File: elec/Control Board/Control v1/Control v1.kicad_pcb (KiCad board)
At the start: 2 copper layers, 126.3 x 160 mm, 194 parts, among them J1 DB9_Female_MountingHoles, J103 Screw_Terminal_01x02, J106 Conn_01x04, J107 Conn_01x07, J11 Screw_Terminal_01x02, J111 Conn_01x08, J13 DB25_Female_MountingHoles, J14 Conn_01x04, J15 Conn_01x05, J16 Conn_01x04, J17 Conn_01x07, J18 Conn_01x04_Pin, J19 RJ12_6P6C_HORZ, J2 Conn_01x08, J20 0.100_2Pin, J201 0.100_2Pin, J202 Conn_01x04, J21 0.100_2Pin, J22 Conn_01x04, J23 0.100_2Pin, J24 0.100_2Pin, J25 Conn_01x04, J3 Conn_01x08, J302 0.100_2Pin, J4 Conn_01x08, J5 Conn_01x08, J6 Conn_01x08, J7 Conn_02x18_Odd_Even, J8 Conn_01x10_MountingPin, J9 Conn_02x12_Odd_Even, Q1 BSS138, Q10 BSS138, Q2 NCE01P30K, Q3 BSS138, Q301 BSS138, Q302 BSS138, Q303 BSS138, Q304 BSS138, Q4 BSS138, Q5 BSS138, Q6 BSS138, Q7 BSS138, Q8 BSS138, Q9 BSS138

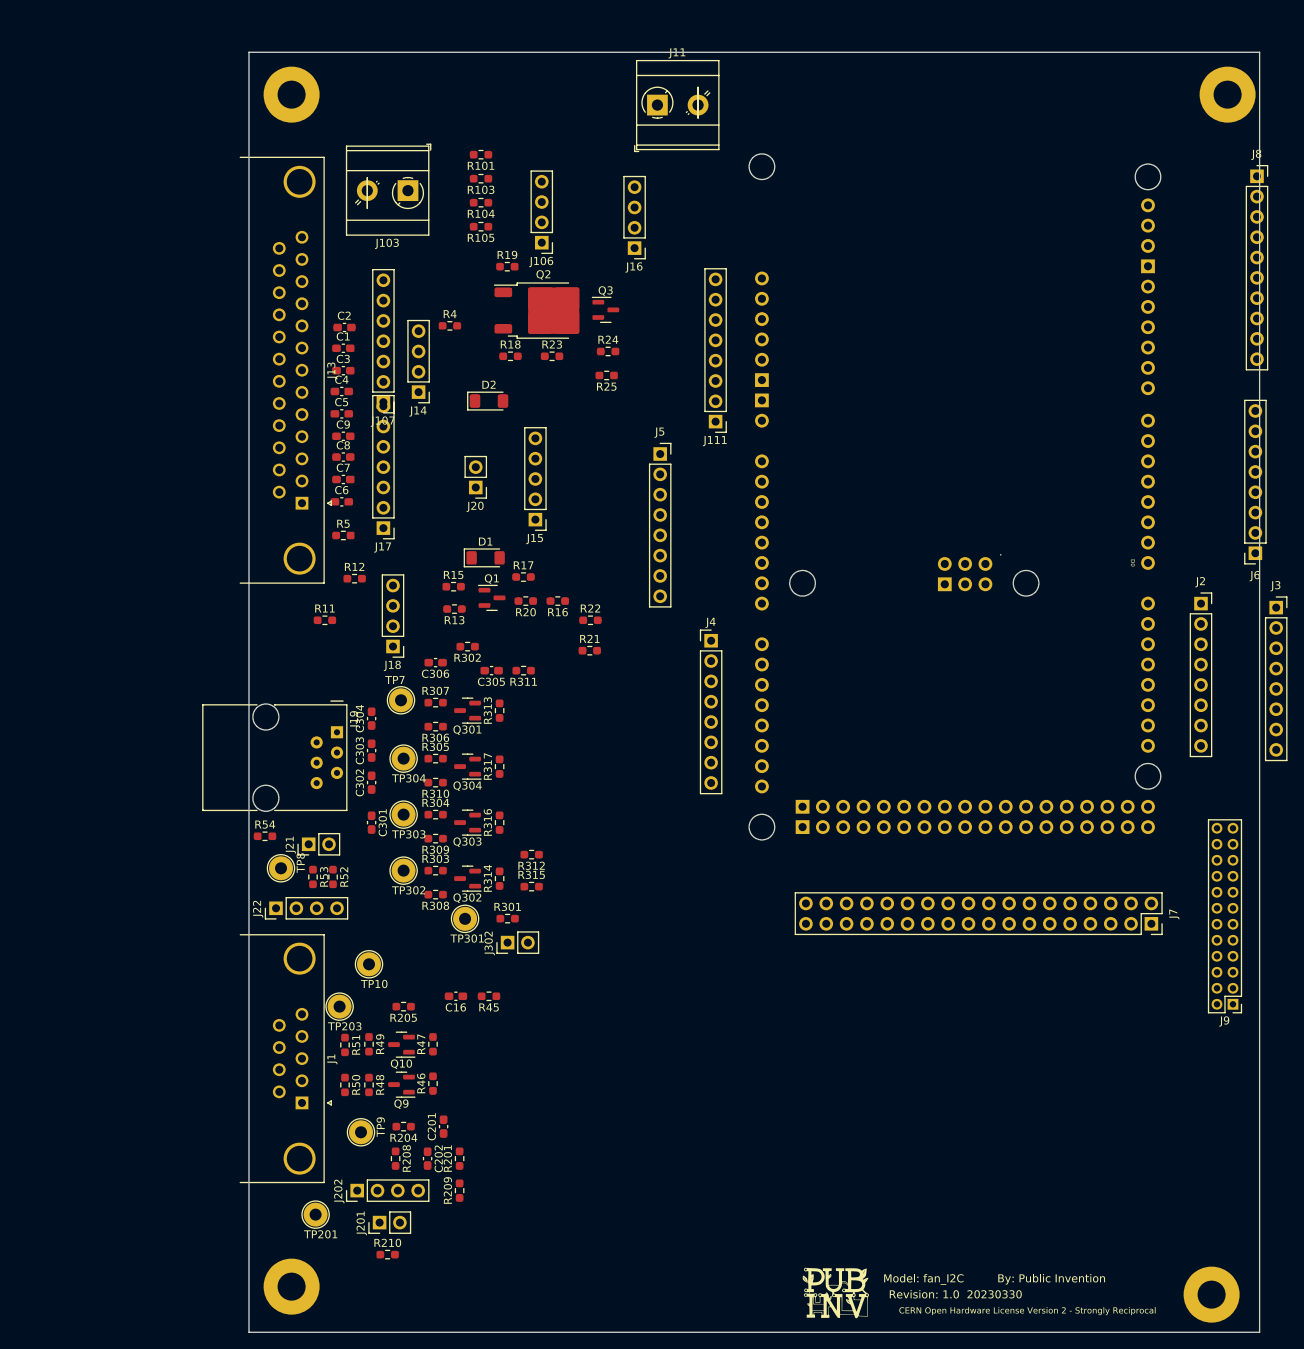
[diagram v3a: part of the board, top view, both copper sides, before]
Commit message: Update schematic for MCP9600 I2C thermocouple.
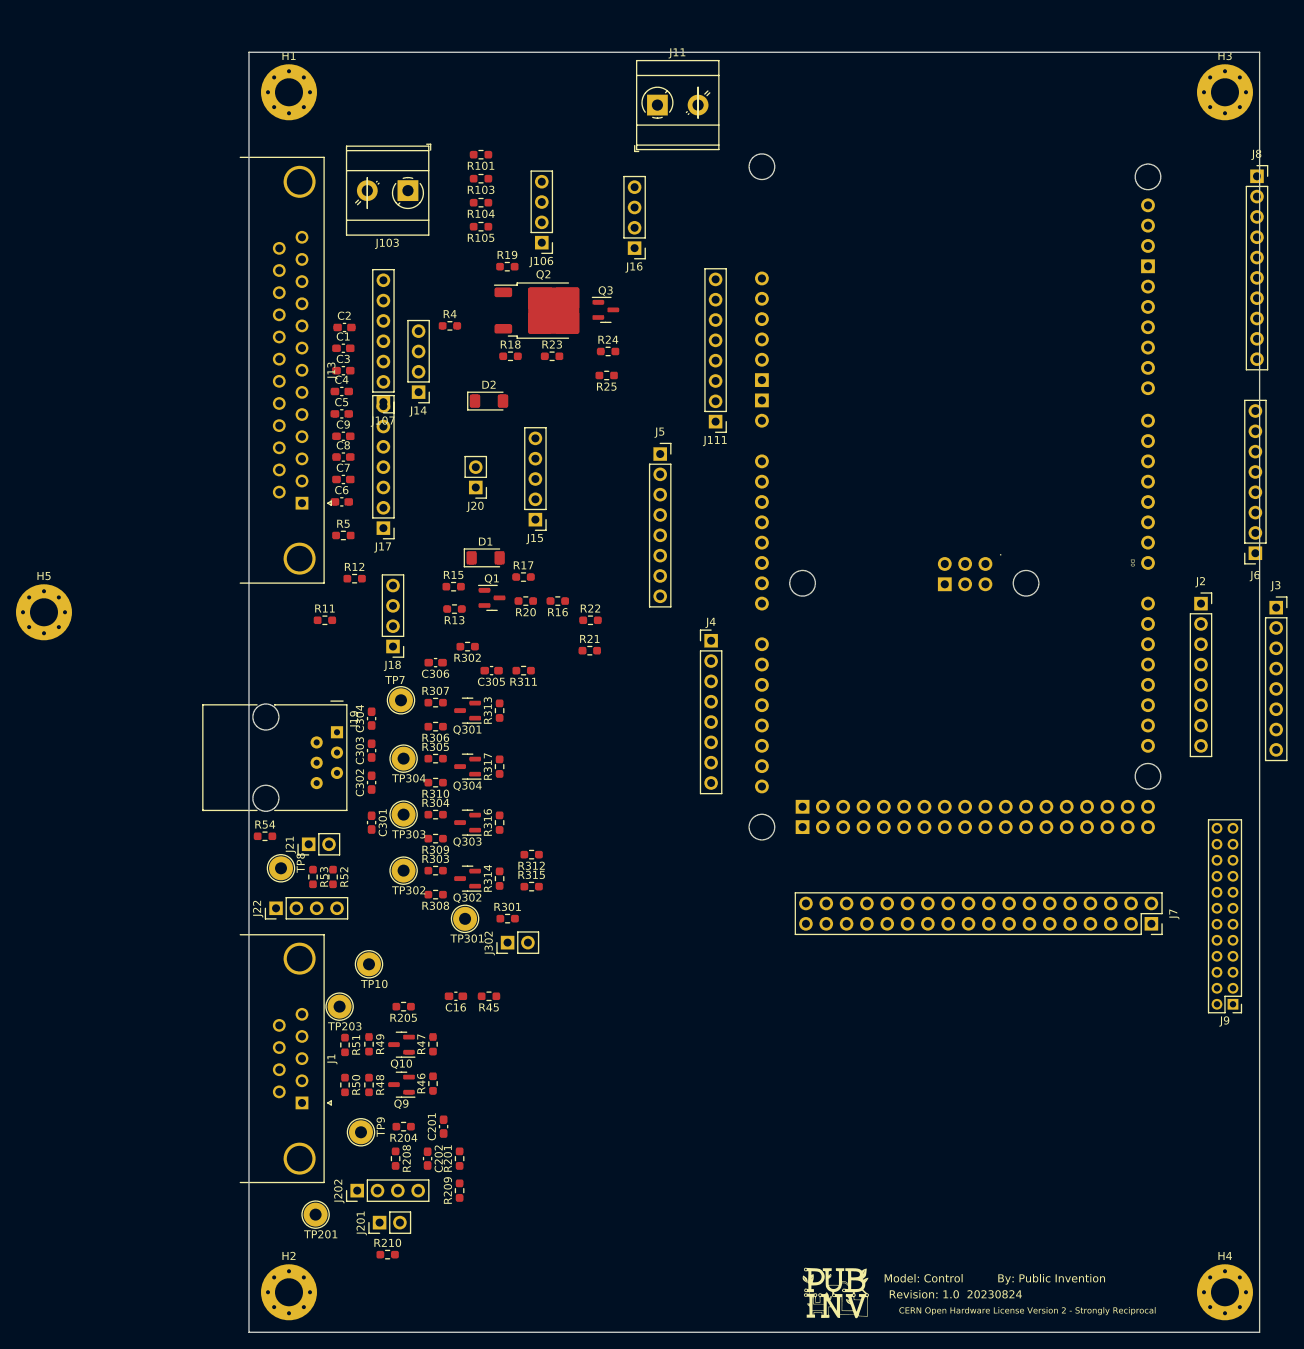
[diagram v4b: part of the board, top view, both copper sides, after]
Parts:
- removed ? (x4): , 
- added H1: MountingHole_Pad_3.5mm, PubInv_KiCad_PCB:MountingHole_3.5mm_Pad_Via, F.Cu at (55.0, 55.0)
- added H2: MountingHole_Pad_3.5mm, PubInv_KiCad_PCB:MountingHole_3.5mm_Pad_Via, F.Cu at (55.0, 205.0)
- added H3: MountingHole_Pad_3.5mm, PubInv_KiCad_PCB:MountingHole_3.5mm_Pad_Via, F.Cu at (172.0, 55.0)
- added H4: MountingHole_Pad_3.5mm, PubInv_KiCad_PCB:MountingHole_3.5mm_Pad_Via, F.Cu at (172.0, 205.0)
- added H5: MountingHole_Pad_3.5mm, PubInv_KiCad_PCB:MountingHole_3.5mm_Pad_Via, F.Cu at (24.4, 120.0)
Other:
- board text added: "Model: Control"
- board text added: "Revision: 1.0 20230824"
- board text removed: "Model: fan_I2C"
- board text removed: "Revision: 1.0 20230330"

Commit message: More update schematic for MCP9600 I2C thermocouple.
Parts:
- added JP14: SolderJumper_3_Bridged12, Jumper:SolderJumper-3_P1.3mm_Bridged12_RoundedPad1.0x1.5mm, F.Cu at (320.3, 113.3)
- added JP15: MAX31850K, PubInv_KiCad_PCB:Adafruit_MAX31850K_Module, F.Cu at (297.4, 148.9)
- added JP16: MAX31855, PubInv_KiCad_PCB:Adafruit_MAX31855_Module, F.Cu at (264.2, 75.2)
- added JP17: MAX31855, PubInv_KiCad_PCB:Adafruit_MAX31855_Module, F.Cu at (286.6, 75.2)
- added JP18: MAX31855, PubInv_KiCad_PCB:Adafruit_MAX31855_Module, F.Cu at (309.0, 75.2)
- added JP19: MCP9600, PubInv_KiCad_PCB:Adafruit_MCP9600_Module, F.Cu at (261.8, 105.8)
- added JP20: MCP9600_, PubInv_KiCad_PCB:Adafruit_MCP9600_Module, F.Cu at (261.8, 128.3)
- added JP21: MCP9600, PubInv_KiCad_PCB:Adafruit_MCP9600_Module, F.Cu at (261.8, 150.8)
- added R10: 1K, Resistor_SMD:R_0603_1608Metric_Pad0.98x0.95mm_HandSolder, F.Cu at (319.6, 116.6)
- added R12: 1K, Resistor_SMD:R_0603_1608Metric_Pad0.98x0.95mm_HandSolder, F.Cu at (319.6, 119.1)
- added R13: 1K, Resistor_SMD:R_0603_1608Metric_Pad0.98x0.95mm_HandSolder, F.Cu at (319.6, 121.6)
- added R14: 1K, Resistor_SMD:R_0603_1608Metric_Pad0.98x0.95mm_HandSolder, F.Cu at (319.6, 124.1)
- added R15: 1K, Resistor_SMD:R_0603_1608Metric_Pad0.98x0.95mm_HandSolder, F.Cu at (319.6, 126.6)
- added R16: 1K, Resistor_SMD:R_0603_1608Metric_Pad0.98x0.95mm_HandSolder, F.Cu at (319.6, 129.2)
- added R17: 1K, Resistor_SMD:R_0603_1608Metric_Pad0.98x0.95mm_HandSolder, F.Cu at (319.6, 131.7)
- added R18: 1K, Resistor_SMD:R_0603_1608Metric_Pad0.98x0.95mm_HandSolder, F.Cu at (319.6, 134.2)
- added R19: 1R0, Resistor_SMD:R_0603_1608Metric_Pad0.98x0.95mm_HandSolder, F.Cu at (269.1, 78.9)
- added R20: 1R0, Resistor_SMD:R_0603_1608Metric_Pad0.98x0.95mm_HandSolder, F.Cu at (290.2, 91.0)
- added TP3: +VccMAX31850_2, TestPoint:TestPoint_Loop_D2.54mm_Drill1.5mm_Beaded, F.Cu at (320.0, 137.9)
- added TP4: +VccMAX31850_3, TestPoint:TestPoint_Loop_D2.54mm_Drill1.5mm_Beaded, F.Cu at (320.0, 143.0)
- added TP5: +VccMAX3185, TestPoint:TestPoint_Loop_D2.54mm_Drill1.5mm_Beaded, F.Cu at (264.4, 80.1)
- added TP6: +VccMCP9600, TestPoint:TestPoint_Loop_D2.54mm_Drill1.5mm_Beaded, F.Cu at (290.6, 87.2)
- JP10, JP9: value MAX31855 -> MAX31850K; footprint PubInv_KiCad_PCB:Adafruit_MAX31855_Module -> PubInv_KiCad_PCB:Adafruit_MAX31850K_Module
- JP11, JP12, JP13: value MAX31865 -> SolderJumper_3_Bridged12; footprint PubInv_KiCad_PCB:Adafruit_MAX31865_Module -> Jumper:SolderJumper-3_P1.3mm_Bridged12_RoundedPad1.0x1.5mm
- JP5, JP6, JP7: value MAX31850K -> SolderJumper_3_Bridged12; footprint PubInv_KiCad_PCB:Adafruit_MAX31850K_Module -> Jumper:SolderJumper-3_P1.3mm_Bridged12_RoundedPad1.0x1.5mm
- JP8: value MAX31855 -> SolderJumper_3_Bridged12; footprint PubInv_KiCad_PCB:Adafruit_MAX31855_Module -> Jumper:SolderJumper-3_P1.3mm_Bridged12_RoundedPad1.0x1.5mm
- moved JP7 91.1 mm to (320.3, 94.1)
- moved JP5 88.6 mm to (320.3, 86.4)
- moved JP6 88.0 mm to (320.3, 90.3)
- moved JP11 59.5 mm to (320.3, 101.8)
- moved JP8 58.3 mm to (320.3, 97.9)
- moved JP12 35.4 mm to (320.3, 105.6)
- moved JP13 22.6 mm to (320.3, 109.5)
- moved JP10 18.0 mm to (297.4, 126.7)
- moved JP9 13.8 mm to (297.4, 104.5)
- moved TP2 13.8 mm to (266.0, 49.0)
- renumbered R10 to R11, R11 to R21, R12 to R22, R13 to R23, R15 to R25, R16 to R26, R17 to R27, R18 to R28, R19 to R29, R20 to R30, R21 to R31, R22 to R32, R23 to R33, R24 to R34, R25 to R35, R26 to R36, R27 to R37, R28 to R38, R29 to R39, R30 to R40, R31 to R41, R32 to R42, R33 to R43, R34 to R44, R35 to R45, R36 to R46, R37 to R47, R38 to R48, R39 to R49, R40 to R50, R41 to R51, R42 to R52, R43 to R53, R44 to R54, R45 to R55, R46 to R56, R47 to R57, R48 to R58, R49 to R59, R7 to R6, R50 to R60, R51 to R61, R52 to R62, R53 to R63, R54 to R64, R6 to R7, TP6 to TP10, TP7 to TP11, TP8 to TP12, TP9 to TP13, TP10 to TP14, TP3 to TP7, TP4 to TP8, TP5 to TP9
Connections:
- JP1 pad 1: GND -> /Thermocouple Amplifier with 1-Wire Breakout Board - MAX31850K/+VccMAX31850
- JP1 pad 3: /Thermocouple Amplifier with 1-Wire Breakout Board - MAX31850K/+VccMAX31850 -> GND
- JP10 pad 1: unconnected-(JP10-Pad1) -> ONE_WIRE_TC
- JP10 pad 2: unconnected-(JP10-Pad2) -> Net-(JP10-Pad2)
- JP10 pad 3: unconnected-(JP10-Pad3) -> Net-(JP10-Pad3)
- JP10 pad 4: unconnected-(JP10-Pad4) -> Net-(JP10-Pad4)
- JP10 pad 5: unconnected-(JP10-Pad5) -> Net-(JP10-Pad5)
- JP10 pad 6: unconnected-(JP10-Pad6) -> Net-(JP10-Pad6)
- JP10 pad 8: (no net) -> GND
- JP11 pad 1: +5V -> GND
- JP11 pad 2: /Thermocouple Amplifier SPI breakout board - MAX31865/+3.3V_MAX31856 -> Net-(JP11-C)
- JP11 pad 3: GND -> /Thermocouple Amplifier with 1-Wire Breakout Board - MAX31850K/+VccMAX31850
- JP12 pad 1: unconnected-(JP12-Pad1) -> GND
- JP12 pad 2: unconnected-(JP12-Pad2) -> Net-(JP12-C)
- JP12 pad 3: unconnected-(JP12-Pad3) -> /Thermocouple Amplifier with 1-Wire Breakout Board - MAX31850K/+VccMAX31850
- JP13 pad 1: unconnected-(JP13-Pad1) -> /Thermocouple Amplifier with 1-Wire Breakout Board - MAX31850K/+VccMAX31850
- JP13 pad 2: unconnected-(JP13-Pad2) -> Net-(JP13-C)
- JP13 pad 3: unconnected-(JP13-Pad3) -> GND
- JP5 pad 1: ONE_WIRE_TC -> GND
- JP5 pad 2: Net-(JP5-Pad2) -> Net-(JP5-C)
- JP5 pad 3: Net-(JP5-Pad3) -> /Thermocouple Amplifier with 1-Wire Breakout Board - MAX31850K/+VccMAX31850
- JP6 pad 1: ONE_WIRE_TC -> /Thermocouple Amplifier with 1-Wire Breakout Board - MAX31850K/+VccMAX31850
- JP6 pad 2: unconnected-(JP6-Pad2) -> Net-(JP6-C)
- JP6 pad 3: unconnected-(JP6-Pad3) -> GND
- JP7 pad 1: ONE_WIRE_TC -> GND
- JP7 pad 2: unconnected-(JP7-Pad2) -> Net-(JP7-C)
- JP7 pad 3: unconnected-(JP7-Pad3) -> /Thermocouple Amplifier with 1-Wire Breakout Board - MAX31850K/+VccMAX31850
- JP8 pad 1: +5V -> GND
- JP8 pad 2: /Thermocouple Amplifier 3wire Interface breakout board - MAX31855 /+3.3V_MAX31855 -> Net-(JP8-C)
- JP8 pad 3: GND -> /Thermocouple Amplifier with 1-Wire Breakout Board - MAX31850K/+VccMAX31850
- JP9 pad 1: unconnected-(JP9-Pad1) -> ONE_WIRE_TC
- JP9 pad 2: unconnected-(JP9-Pad2) -> Net-(JP9-Pad2)
- JP9 pad 3: unconnected-(JP9-Pad3) -> Net-(JP9-Pad3)
- JP9 pad 4: unconnected-(JP9-Pad4) -> Net-(JP9-Pad4)
- JP9 pad 5: unconnected-(JP9-Pad5) -> Net-(JP9-Pad5)
- JP9 pad 6: unconnected-(JP9-Pad6) -> Net-(JP9-Pad6)
- JP9 pad 8: (no net) -> GND
- R11 pad 2: Net-(JP5-Pad5) -> Net-(JP9-Pad5)
- R7 pad 2: Net-(JP5-Pad2) -> Net-(JP9-Pad2)
- R8 pad 2: Net-(JP5-Pad3) -> Net-(JP9-Pad3)
- R9 pad 2: Net-(JP5-Pad4) -> Net-(JP9-Pad4)
- TP2 pad 1: Net-(JP5-Pad6) -> Net-(JP9-Pad6)

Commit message: Next and place thermocouple boards.
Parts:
- removed C201, C202, C305, C306: 1uF, Capacitor_SMD:C_0603_1608Metric_Pad1.08x0.95mm_HandSolder
- removed C301, C302, C303, C304: 39PF, Capacitor_SMD:C_0603_1608Metric_Pad1.08x0.95mm_HandSolder
- removed H10, H11, H6, H7, H8, H9: MountingHole_Pad_3.5mm, PubInv_KiCad_PCB:MountingHole_3.5mm_Pad_Via
- removed J103: Screw_Terminal_01x02, TerminalBlock_MetzConnect:TerminalBlock_MetzConnect_Type073_RT02602HBLU_1x02_P5.08mm_Horizontal
- removed J106, J202, J25: Conn_01x04, Connector_PinHeader_2.54mm:PinHeader_1x04_P2.54mm_Vertical
- removed J107: Conn_01x07, Connector_PinHeader_2.54mm:PinHeader_1x07_P2.54mm_Vertical
- removed J111: Conn_01x08, Connector_PinHeader_2.54mm:PinHeader_1x08_P2.54mm_Vertical
- removed J201, J23, J24, J302: 0.100_2Pin, Connector_PinHeader_2.54mm:PinHeader_1x02_P2.54mm_Vertical
- removed Q301, Q302, Q303, Q304: BSS138, Package_TO_SOT_SMD:SOT-23
- removed R101, R103, R104, R105: 540R, Resistor_SMD:R_0603_1608Metric_Pad0.98x0.95mm_HandSolder
- removed R201, R208, R301, R302, R311: 1R, Resistor_SMD:R_0603_1608Metric_Pad0.98x0.95mm_HandSolder
- removed R204, R205, R308, R313, R316, R317: 10K, Resistor_SMD:R_0603_1608Metric_Pad0.98x0.95mm_HandSolder
- removed R209, R210, R303, R304, R305, R307, R312, R315: DNI, Resistor_SMD:R_0603_1608Metric_Pad0.98x0.95mm_HandSolder
- removed R306, R309, R310, R314: 1K, Resistor_SMD:R_0603_1608Metric_Pad0.98x0.95mm_HandSolder
- removed TP201: I2C_VCC, TestPoint:TestPoint_Loop_D2.54mm_Drill1.5mm_Beaded
- removed TP203: SDA_5V, TestPoint:TestPoint_Loop_D2.54mm_Drill1.5mm_Beaded
- removed TP301: ControllerVCC, TestPoint:TestPoint_Loop_D2.54mm_Drill1.5mm_Beaded
- removed TP302: CPIO, TestPoint:TestPoint_Loop_D2.54mm_Drill1.5mm_Beaded
- removed TP303: SCK, TestPoint:TestPoint_Loop_D2.54mm_Drill1.5mm_Beaded
- removed TP304: COPI, TestPoint:TestPoint_Loop_D2.54mm_Drill1.5mm_Beaded
- added J12: Screw_Terminal_01x02, TerminalBlock_TE-Connectivity:TerminalBlock_TE_282834-2_1x02_P2.54mm_Horizontal, F.Cu at (80.5, 56.0)
- added S1: SWITCH_TACTILE_SPST-NO_0.05A_24V, PubInv_KiCad_PCB:Switch_Tactile_THT_6x6mm, F.Cu at (95.0, 53.2)
- added TP15: Due_5V2, TestPoint:TestPoint_Loop_D2.54mm_Drill1.5mm_Beaded, F.Cu at (95.7, 62.1)
- J11: footprint TerminalBlock_MetzConnect:TerminalBlock_MetzConnect_Type073_RT02602HBLU_1x02_P5.08mm_Horizontal -> TerminalBlock_TE-Connectivity:TerminalBlock_TE_282834-2_1x02_P2.54mm_Horizontal
- moved JP11 239.1 mm to (91.0, 169.6), turned to 90 degrees
- moved TP4 236.0 mm to (86.0, 174.3), turned to 180 degrees
- moved JP12 234.4 mm to (94.8, 169.6), turned to 90 degrees
- moved JP18 233.3 mm to (104.4, 187.4), turned to 180 degrees
- moved R18 230.5 mm to (92.8, 175.5), turned to -90 degrees
- moved JP13 229.6 mm to (98.7, 169.6), turned to -90 degrees
- moved R17 227.1 mm to (96.8, 175.4), turned to -90 degrees
- moved JP14 225.0 mm to (102.5, 169.6), turned to 90 degrees
- moved R16 224.6 mm to (99.8, 175.4), turned to -90 degrees
- moved R15 222.2 mm to (102.8, 175.4), turned to -90 degrees
- moved JP5 218.0 mm to (117.8, 167.3), turned to 90 degrees
- moved JP6 213.1 mm to (121.7, 167.3), turned to -90 degrees
- moved TP3 208.8 mm to (114.2, 172.8), turned to 180 degrees
- moved JP7 208.1 mm to (125.5, 167.3), turned to 90 degrees
- moved R14 204.6 mm to (121.0, 172.9), turned to -90 degrees
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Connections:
- A1 pad 5V2: unconnected-(A1-SPI_5V-Pad5V2) -> Net-(A1-SPI_5V)
- A1 pad GND4: unconnected-(A1-SPI_GND-PadGND4) -> GND
- A1 pad RST2: unconnected-(A1-SPI_RESET-PadRST2) -> Net-(A1-SPI_RESET)
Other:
- board text added: "locked"
- board text removed: "CERN Open Hardware License Version 2 - Strongly Reciprocal"
- board text removed: "Model: Control"
- board text removed: "Revision: 1.0 20230824"

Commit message: Fix swome ERC errors.
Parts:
- added J9: Conn_01x10, Connector_PinSocket_2.54mm:PinSocket_1x10_P2.54mm_Vertical, F.Cu at (167.5, 169.4)
- added R1: 1R0, Resistor_SMD:R_0603_1608Metric_Pad0.98x0.95mm_HandSolder, F.Cu at (136.4, 79.6)
- added R2: 1R0, Resistor_SMD:R_0603_1608Metric_Pad0.98x0.95mm_HandSolder, F.Cu at (136.4, 82.1)
- added R3: 1R0, Resistor_SMD:R_0603_1608Metric_Pad0.98x0.95mm_HandSolder, F.Cu at (136.4, 84.6)
- added R32: DNI, Resistor_SMD:R_0603_1608Metric_Pad0.98x0.95mm_HandSolder, F.Cu at (87.0, 123.3)
- added R4: 1R0, Resistor_SMD:R_0603_1608Metric_Pad0.98x0.95mm_HandSolder, F.Cu at (136.4, 87.1)
- added R5: 1R0, Resistor_SMD:R_0603_1608Metric_Pad0.98x0.95mm_HandSolder, F.Cu at (136.4, 89.6)
- added R6: 1R0, Resistor_SMD:R_0603_1608Metric_Pad0.98x0.95mm_HandSolder, F.Cu at (136.4, 92.2)
- added R7: 1R0, Resistor_SMD:R_0603_1608Metric_Pad0.98x0.95mm_HandSolder, F.Cu at (136.4, 94.7)
- added R8: 1R, Resistor_SMD:R_0603_1608Metric_Pad0.98x0.95mm_HandSolder, F.Cu at (136.4, 97.2)
- J8: value Conn_01x10_MountingPin -> Conn_01x10
- moved J8 2.16 mm to (169.0, 67.1)
- moved J13 0.50 mm to (80.4, 55.5)
- moved JP9 0.20 mm to (158.5, 178.4)
- renumbered J9 to J10, J11 to J12, J12 to J13, J13 to J15, J14 to J16, J15 to J17, J16 to J18, J17 to J19, J18 to J20, J19 to J21, J20 to J22, J21 to J23, J22 to J24, R2 to R10, R3 to R11, R4 to R12, R5 to R13, R6 to R14, R7 to R15, R8 to R16, R9 to R17, R10 to R18, R11 to R19, R12 to R20, R13 to R21, R14 to R22, R15 to R23, R16 to R24, R17 to R25, R18 to R26, R19 to R27, R20 to R28, R21 to R29, R22 to R30, R23 to R31, R25 to R33, R26 to R34, R27 to R35, R28 to R36, R29 to R37, R30 to R38, R31 to R39, R32 to R40, R33 to R41, R34 to R42, R35 to R43, R36 to R44, R37 to R45, R38 to R46, R39 to R47, R40 to R48, R41 to R49, R42 to R50, R43 to R51, R44 to R52, R45 to R53, R46 to R54, R47 to R55, R48 to R56, R49 to R57, R50 to R58, R51 to R59, R52 to R60, R53 to R61, R54 to R62, R55 to R63, R56 to R64, R57 to R65, R58 to R66, R59 to R67, R60 to R68, R61 to R69, R62 to R70, R63 to R71, R64 to R72, R1 to R9, TP15 to TP1, TP9 to TP10, TP10 to TP11, TP11 to TP12, TP12 to TP13, TP13 to TP14, TP14 to TP15, TP1 to TP2, TP2 to TP3, TP3 to TP4, TP4 to TP5, TP5 to TP6, TP6 to TP7, TP7 to TP8, TP8 to TP9
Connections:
- J23 pad 2: /I2C_LevelShift/+12forSPIPeripherial -> +12V
- R33 pad 2: /Blower controller/+5VFan -> +5V
- R34 pad 2: /Blower controller/+3.3VFan -> +3.3V
- R38 pad 1: /Blower controller/+3.3VFan -> +3.3V
- R63 pad 1: /I2C_LevelShift/+3V3LevelShift -> +3.3V
- R70 pad 2: /I2C_LevelShift/+5LevelShift -> +5V
- R71 pad 2: /I2C_LevelShift/+5LevelShift -> +5V
- R72 pad 2: /I2C_LevelShift/+12forSPIPeripherial -> +12V
